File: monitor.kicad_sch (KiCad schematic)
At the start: 54 parts, among them J1 USB_C_Plug, J2 USB_C_Receptacle_USB2.0_14P, J3 Display, J4 Program, J5 Boot, U1 STM32U031K8Ux, U2 TPSM365R6V3RDNR, U3 TMP117xxDRV, U4 REF5025ADGK, U5 CC6903, Y1 32768Hz

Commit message: First cut of some code
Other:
- note added: "0x92 / 0x49 address."
- note removed: "0x90 / 0x48 address."
- moved on the sheet: C1, R1, R2
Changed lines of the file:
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@@
 	(generator_version "9.0")
 	(paper "A4")
-	(text "0x90 / 0x48 address."
+	(text "0x92 / 0x49 address."
 		(exclude_from_sim no)
 		(at 155.956 133.35 0)
@@
 	)
 	(junction
-		(at 134.62 52.07)
+		(at 135.89 53.34)
 		(diameter 0)
 		(color 0 0 0 0)
@@
 	)
 	(junction
-		(at 128.27 52.07)
+		(at 129.54 53.34)
 		(diameter 0)
 		(color 0 0 0 0)
@@
 	)
 	(junction
-		(at 128.27 60.96)
+		(at 129.54 62.23)
 		(diameter 0)
 		(color 0 0 0 0)
@@
 	(wire
 		(pts
-			(xy 128.27 60.96) (xy 134.62 60.96)
+			(xy 129.54 62.23) (xy 135.89 62.23)
 		)
 		(stroke
@@
 	(wire
 		(pts
-			(xy 134.62 52.07) (xy 134.62 53.34)
+			(xy 135.89 53.34) (xy 135.89 54.61)
 		)
 		(stroke
@@
 	(wire
 		(pts
-			(xy 128.27 52.07) (xy 134.62 52.07)
+			(xy 129.54 53.34) (xy 135.89 53.34)
 		)
 		(stroke
@@
 	(wire
 		(pts
-			(xy 128.27 52.07) (xy 128.27 53.34)
+			(xy 129.54 53.34) (xy 129.54 54.61)
 		)
 		(stroke
@@
 	(wire
 		(pts
-			(xy 134.62 52.07) (xy 137.16 52.07)
+			(xy 135.89 53.34) (xy 138.43 53.34)
 		)
 		(stroke
@@
 	(wire
 		(pts
-			(xy 114.3 52.07) (xy 120.65 52.07)
+			(xy 115.57 53.34) (xy 121.92 53.34)
 		)
 		(stroke
@@
 	)
 	(label "Vout"
-		(at 114.3 52.07 0)
+		(at 115.57 53.34 0)
 		(effects
 			(font
@@
 	)
 	(label "VSense"
-		(at 137.16 52.07 180)
+		(at 138.43 53.34 180)
 		(effects
 			(font
@@
 	(symbol
 		(lib_id "Device:R")
-		(at 128.27 57.15 0)
+		(at 129.54 58.42 0)
 		(unit 1)
 		(exclude_from_sim no)
@@
 		(dnp no)
 		(property "Reference" "R2"
-			(at 127 57.1499 90)
+			(at 128.27 58.4199 90)
 			(do_not_autoplace yes)
 			(effects
@@
 		)
 		(property "Value" "18k"
-			(at 128.27 57.1499 90)
+			(at 129.54 58.4199 90)
 			(effects
 				(font
@@
 		)
 		(property "Footprint" "Resistor_SMD:R_0402_1005Metric"
-			(at 126.492 57.15 90)
+			(at 127.762 58.42 90)
 			(effects
 				(font
@@
 		)
 		(property "Datasheet" "~"
-			(at 128.27 57.15 0)
+			(at 129.54 58.42 0)
 			(effects
 				(font
@@
 		)
 		(property "Description" "Resistor"
-			(at 128.27 57.15 0)
+			(at 129.54 58.42 0)
 			(effects
 				(font
@@
 		)
 		(property "JLCPCB" "C25762"
-			(at 128.27 57.15 0)
+			(at 129.54 58.42 0)
 			(effects
 				(font
@@
 	(symbol
 		(lib_id "power:GND")
-		(at 128.27 60.96 0)
+		(at 129.54 62.23 0)
 		(unit 1)
 		(exclude_from_sim no)
@@
 		(dnp no)
 		(property "Reference" "#PWR053"
-			(at 128.27 67.31 0)
+			(at 129.54 68.58 0)
 			(effects
 				(font
@@
 		)
 		(property "Value" "GND"
-			(at 128.27 64.516 0)
+			(at 129.54 65.786 0)
 			(effects
 				(font
@@
 		)
 		(property "Footprint" ""
-			(at 128.27 60.96 0)
+			(at 129.54 62.23 0)
 			(effects
 				(font
@@
 		)
 		(property "Datasheet" ""
-			(at 128.27 60.96 0)
+			(at 129.54 62.23 0)
 			(effects
 				(font
@@
 		)
 		(property "Description" "Power symbol creates a global label with name \"GND\" , ground"
-			(at 128.27 60.96 0)
+			(at 129.54 62.23 0)
 			(effects
 				(font
@@
 	(symbol
 		(lib_id "Device:C")
-		(at 134.62 57.15 0)
+		(at 135.89 58.42 0)
 		(unit 1)
 		(exclude_from_sim no)
@@
 		(dnp no)
 		(property "Reference" "C1"
-			(at 135.128 55.1179 0)
+			(at 136.398 56.3879 0)
 			(effects
 				(font
@@
 		)
 		(property "Value" "10u"
-			(at 135.382 59.4359 0)
+			(at 136.652 60.7059 0)
 			(effects
 				(font
@@
 		)
 		(property "Footprint" "Capacitor_SMD:C_0402_1005Metric"
-			(at 135.5852 60.96 0)
+			(at 136.8552 62.23 0)
 			(effects
 				(font
@@
 		)
 		(property "Datasheet" "~"
-			(at 134.62 57.15 0)
+			(at 135.89 58.42 0)
 			(effects
 				(font
@@
 		)
 		(property "Description" "Unpolarized capacitor"
-			(at 134.62 57.15 0)
+			(at 135.89 58.42 0)
 			(effects
 				(font
@@
 		)
 		(property "JLCPCB" "C15525"
-			(at 134.62 57.15 0)
+			(at 135.89 58.42 0)
 			(effects
 				(font
@@
 	(symbol
 		(lib_id "Device:R")
-		(at 124.46 52.07 90)
+		(at 125.73 53.34 90)
 		(mirror x)
 		(unit 1)
@@
 		(dnp no)
 		(property "Reference" "R1"
-			(at 124.4599 50.8 90)
+			(at 125.7299 52.07 90)
 			(do_not_autoplace yes)
 			(effects
@@
 		)
 		(property "Value" "100k"
-			(at 124.4599 52.07 90)
+			(at 125.7299 53.34 90)
 			(effects
 				(font
@@
 		)
 		(property "Footprint" "Resistor_SMD:R_0402_1005Metric"
-			(at 124.46 50.292 90)
+			(at 125.73 51.562 90)
 			(effects
 				(font
@@
 		)
 		(property "Datasheet" "~"
-			(at 124.46 52.07 0)
+			(at 125.73 53.34 0)
 			(effects
 				(font
@@
 		)
 		(property "Description" "Resistor"
-			(at 124.46 52.07 0)
+			(at 125.73 53.34 0)
 			(effects
 				(font
@@
 		)
 		(property "JLCPCB" "C25741"
-			(at 124.46 52.07 0)
+			(at 125.73 53.34 0)
 			(effects
 				(font

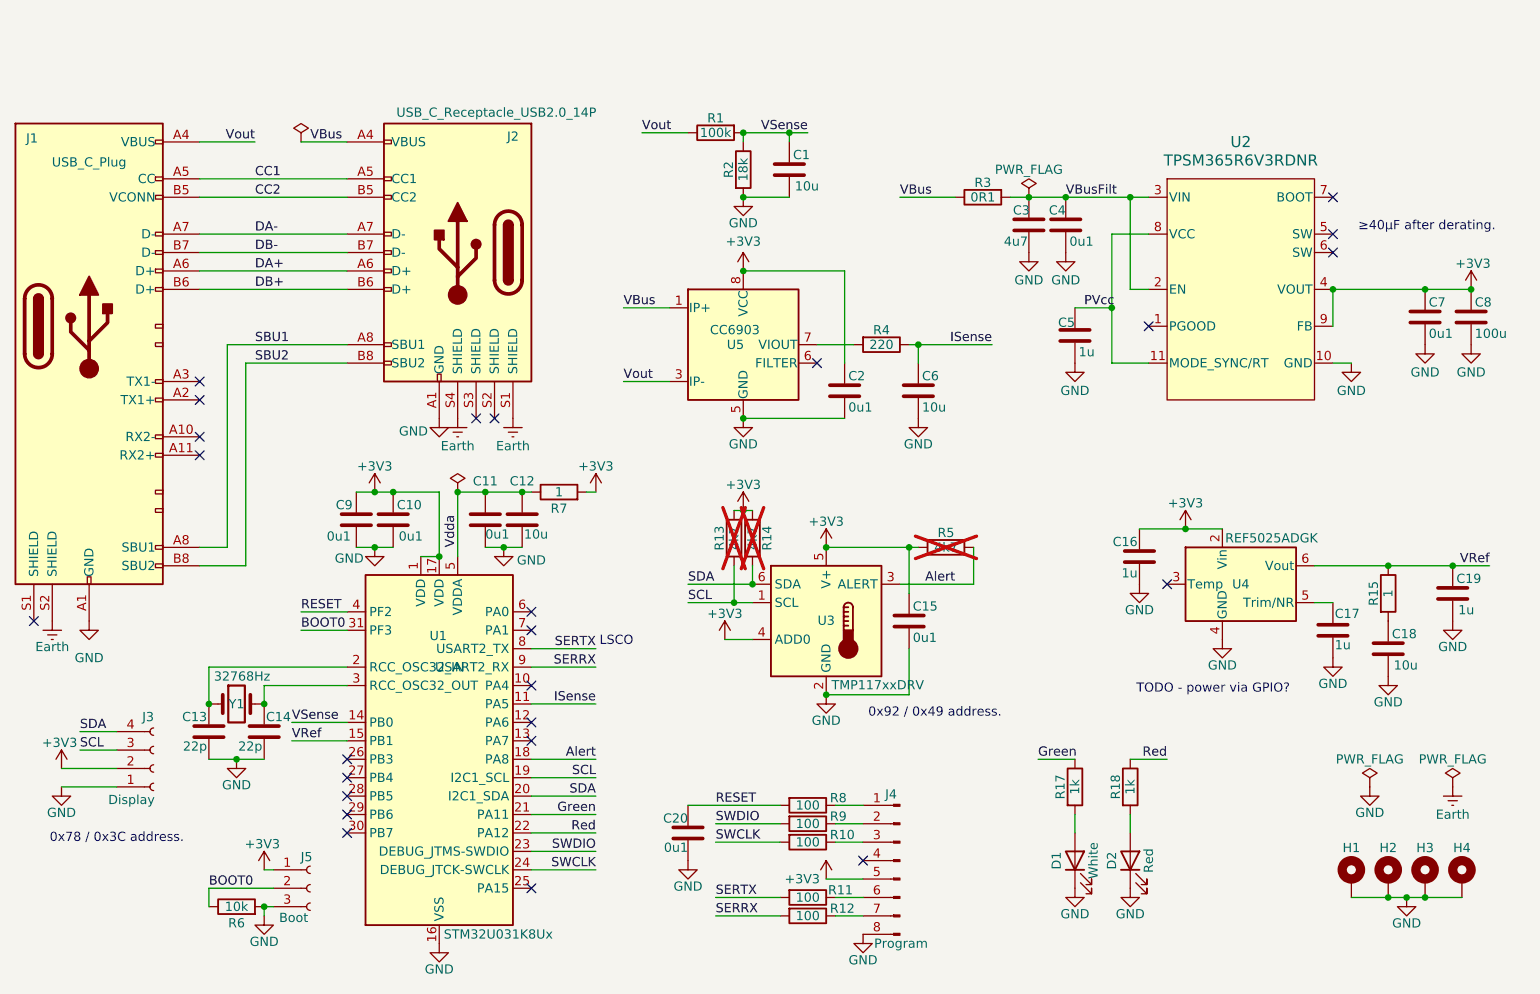
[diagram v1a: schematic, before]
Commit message: Big update to the monitor.
Accell, low side current sense.
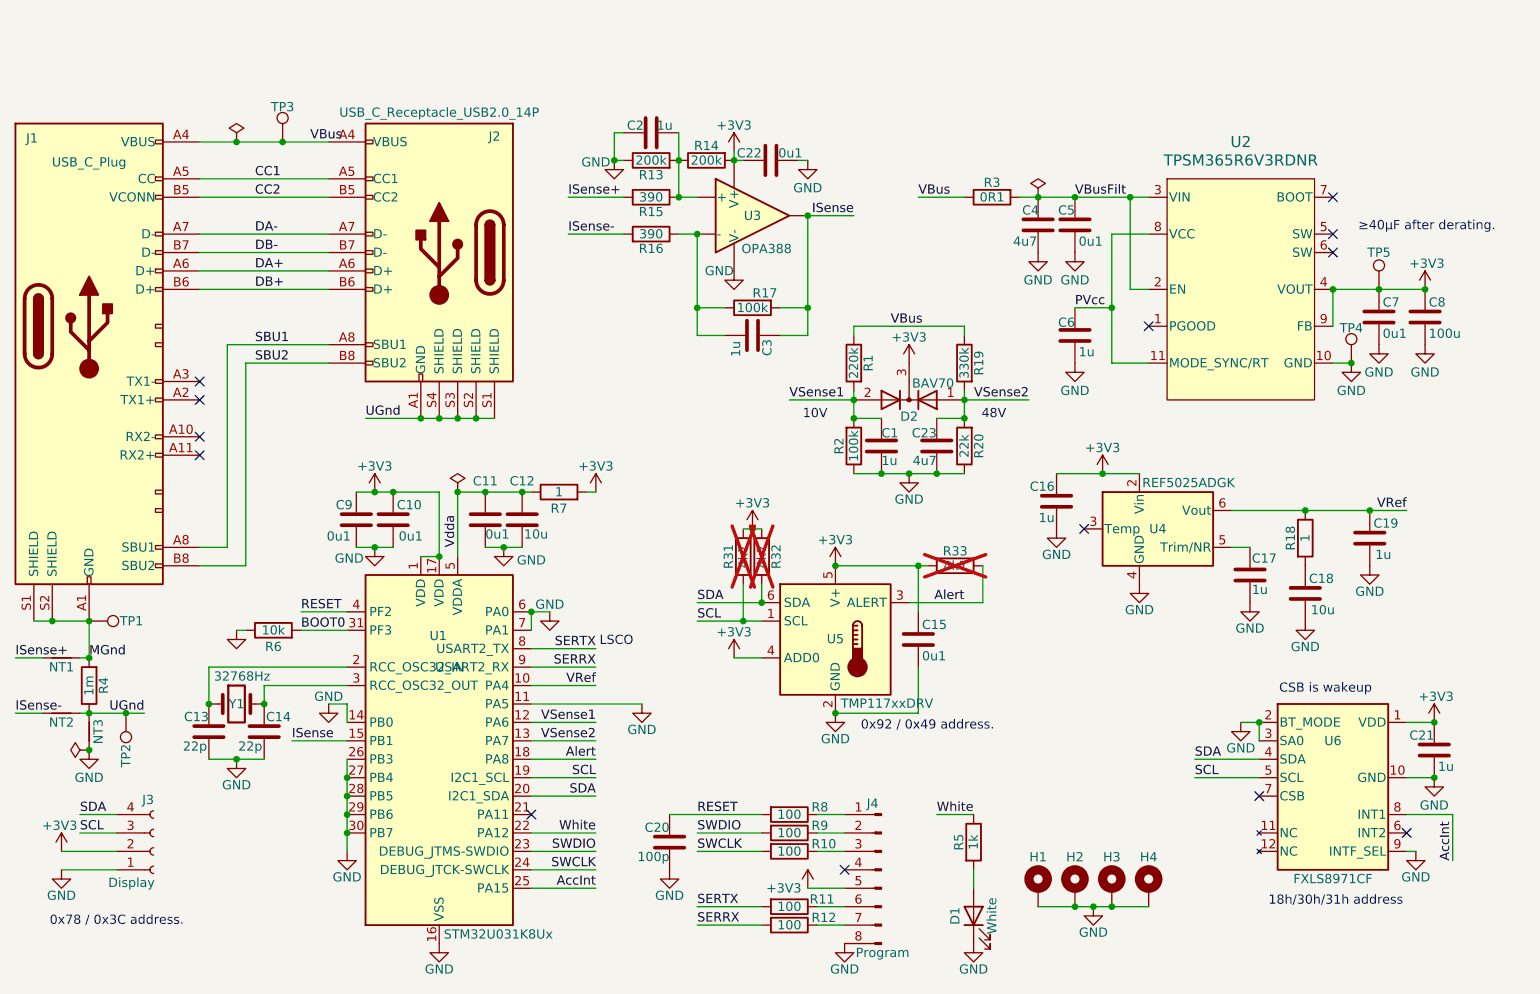
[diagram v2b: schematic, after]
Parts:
- removed C6: 10u, Capacitor_SMD:C_0402_1005Metric, symbol Device:C
- removed D2: Red, LED_SMD:LED_0603_1608Metric, symbol Device:LED
- removed J5: Boot, Parts:PinHeader_1x03_P2.54mm_Vertical, symbol Connector:Conn_01x03_Socket
- removed R18: 1k, Resistor_SMD:R_0402_1005Metric, symbol Device:R
- removed U5: CC6903, Package_SO:SOIC-8_3.9x4.9mm_P1.27mm, symbol Parts:CC6903
- added C21, C3: 1u, Capacitor_SMD:C_0402_1005Metric, symbol Device:C
- added C22: 0u1, Capacitor_SMD:C_0402_1005Metric, symbol Device:C
- added C23: 4u7, Capacitor_SMD:C_0402_1005Metric, symbol Device:C
- added D2: BAV70, Package_TO_SOT_SMD:SOT-23, symbol Diode:BAV70
- added NT1, NT2: NetTie_2, Parts:NetTie-2_0.2mm, symbol Parts:NetTie_2
- added NT3: NetTie_2, NetTie:NetTie-2_SMD_Pad0.5mm, symbol Parts:NetTie_2
- added R13, R14: 200k, Resistor_SMD:R_0603_1608Metric, symbol Device:R
- added R15, R16: 390, Resistor_SMD:R_0603_1608Metric, symbol Device:R
- added R17: 100k, Resistor_SMD:R_0603_1608Metric, symbol Device:R
- added R19: 330k, Resistor_SMD:R_0603_1608Metric, symbol Device:R
- added R20: 22k, Resistor_SMD:R_0603_1608Metric, symbol Device:R
- added TP1, TP2, TP3, TP4, TP5: TestPoint, Parts:TestPoint, symbol Connector:TestPoint
- added U3: OPA388, Package_TO_SOT_SMD:SOT-23-5, symbol Parts:OPA388
- added U6: FXLS8971CF, Parts:FXLS8971CF, symbol Parts:FXLS8971CF
- C1: value 10u -> 1u; JLCPCB C15525 -> (none)
- C2: value 0u1 -> 1u; JLCPCB C307331 -> (none)
- C20: value 0u1 -> 100p; JLCPCB C307331 -> C1546
- J3: footprint Parts:PinHeader_1x04_P2.54mm_Vertical -> Parts:JST_XH_B4B-XH-A_1x04_P2.50mm_Vertical
- R1: value 100k -> 220k; footprint Resistor_SMD:R_0402_1005Metric -> Resistor_SMD:R_0603_1608Metric; JLCPCB C25741 -> (none)
- R18: renamed from R15; footprint Resistor_SMD:R_0603_1608Metric -> Resistor_SMD:R_0402_1005Metric; JLCPCB C22936 -> C25086
- R2: value 18k -> 100k; footprint Resistor_SMD:R_0402_1005Metric -> Resistor_SMD:R_0603_1608Metric; JLCPCB C25762 -> (none)
- R4: value 220 -> 1m; footprint Resistor_SMD:R_0402_1005Metric -> Resistor_SMD:R_1206_3216Metric; JLCPCB C25091 -> (none)
- U1: now in the parts list
- renumbered C3 to C4, C4 to C5, C5 to C6, R13 to R31, R14 to R32, R5 to R33, R17 to R5, U3 to U5
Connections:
- net Vout is gone; now on net VBus: J1.A4 (VBUS), J1.A9 (VBUS), J1.B4 (VBUS), J1.B9 (VBUS), R1.1
- net +3V3: now also C21.1, C22.2, D2.3 (K), R14.2, TP5.1, U3.5 (V+), U6.1 (VDD); no longer C2.1
- net BOOT0: now also R6.2; no longer R6.1
- net GND: now also C2.1, R2.1, R6.1, U1.11 (PA5), U1.14 (PB0), U1.26 (PB3), U1.27 (PB4), U1.28 (PB5), U1.29 (PB6), U1.30 (PB7), U1.6 (PA0), U1.7 (PA1), C21.2, C22.1, C23.2, NT3.1, R13.1, R20.1, TP4.1, U3.2 (V-), U6.10 (GND), U6.2 (BT_MODE), U6.3 (SA0), U6.9 (INTF_SEL); no longer C2.2, J1.A1 (GND), J1.A12 (GND), J1.B1 (GND), J1.B12 (GND), J2.A1 (GND), J2.A12 (GND), J2.B1 (GND), J2.B12 (GND), R2.2, R6.2
- net ISense: now also U1.15 (PB1), C3.1, R17.2, U3.1; no longer R4.1, U1.11 (PA5)
- net SCL: now also U6.5 (SCL)
- net SDA: now also U6.4 (SDA)
- net VBus: now also R19.1, TP3.1
- net VRef: now also U1.10 (PA4); no longer U1.15 (PB1)
- net UGnd: now reaches J2.S2 (SHIELD)
- net UGnd: now also J2.A1 (GND), J2.A12 (GND), J2.B1 (GND), J2.B12 (GND), J2.S1 (SHIELD), J2.S3 (SHIELD), J2.S4 (SHIELD), R4.1, NT2.1, NT3.2, TP2.1
- net VSense1: now reaches U1.12 (PA6)
- net VSense1: now also C1.1, R1.2, R2.2, D2.2 (A)
- net VSense2: now reaches U1.13 (PA7)
- net VSense2: now also C23.1, D2.1 (A), R19.2, R20.2
- net AccInt: now reaches U1.25 (PA15)
- net AccInt: now also U6.8 (INT1)
- net MGnd: now reaches R4.2
- net MGnd: now also J1.A1 (GND), J1.A12 (GND), J1.B1 (GND), J1.B12 (GND), J1.S1 (SHIELD), J1.S2 (SHIELD), NT1.1, TP1.1
- removed net Earth: J1.S2 (SHIELD), J2.S1 (SHIELD), J2.S4 (SHIELD)
- net Green: no longer names the net of U1.21 (PA11)
- net Green: no longer R5.1
- net Red renamed White
- net White: now also R5.1
- removed net VSense: C1.1, R1.2, R2.1, U1.14 (PB0)
- new net: C2.2, R13.2, R14.1, R15.1, U3.3 (+)
- new net: C3.2, R16.1, R17.1, U3.4 (-)
- new net ISense+: NT1.2, R15.2
- new net ISense-: NT2.2, R16.2
- no-connect marks 25 -> 13
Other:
- note added: "10V"
- note added: "18h/30h/31h address"
- note added: "48V"
- note added: "CSB is wakeup"
- note removed: "TODO - power via GPIO?"
- moved on the sheet: C1, C15, C16, C17, C18, C19, C20, C4, C5, C7, C8, D1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

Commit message: Switch to the 2-stage sense amp.
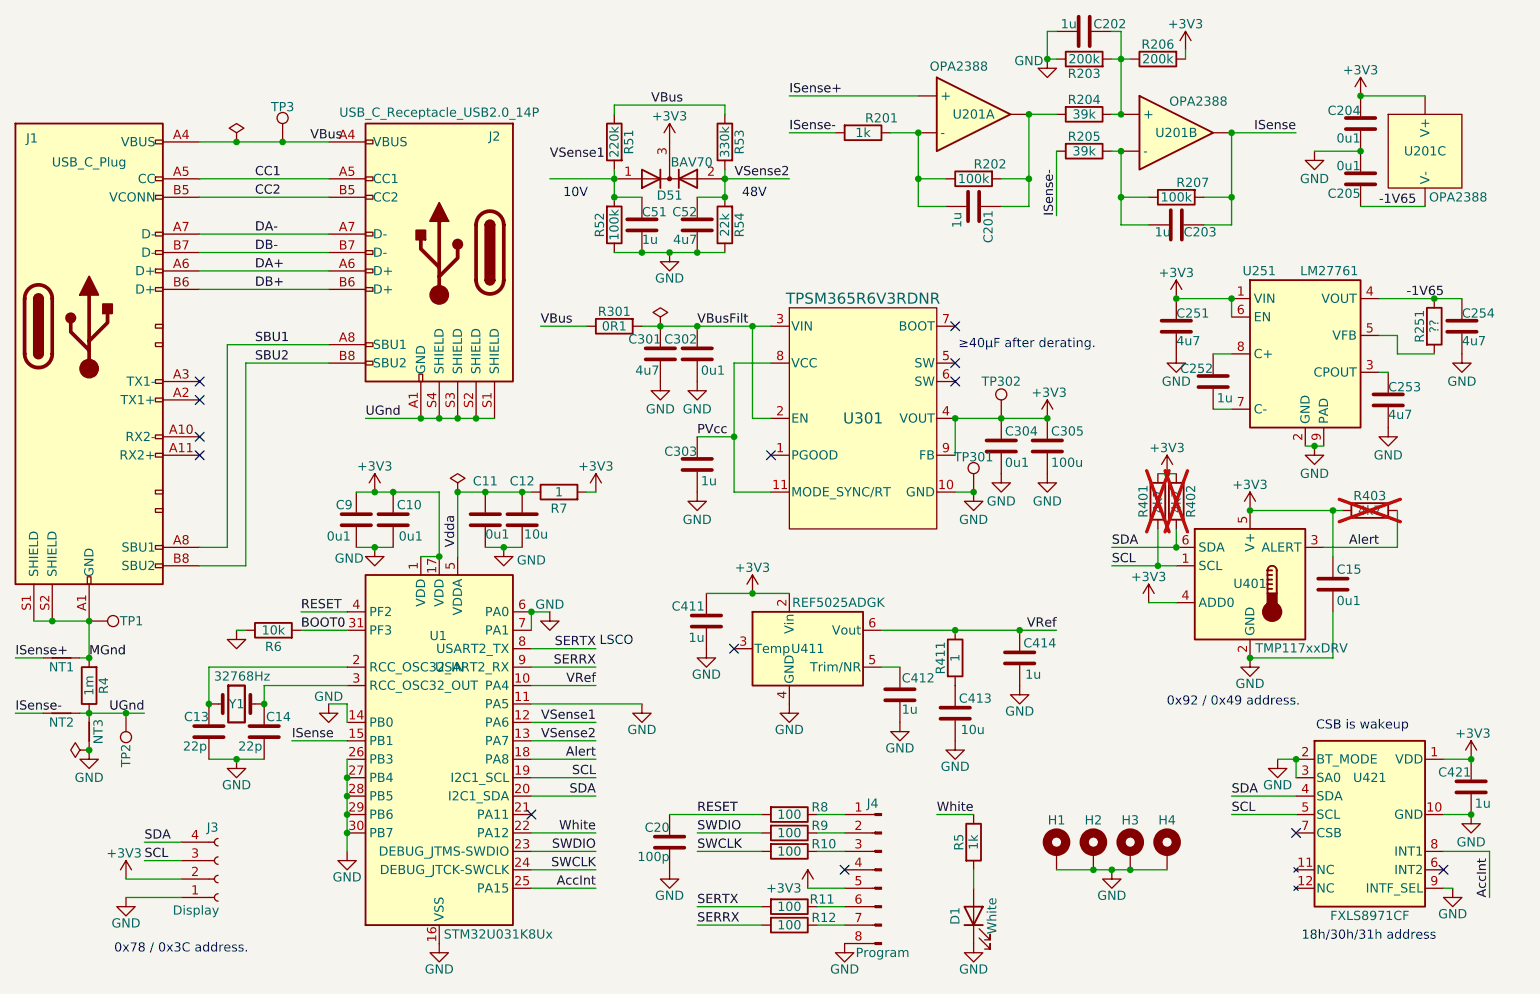
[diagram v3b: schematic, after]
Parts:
- removed C22: 0u1, Capacitor_SMD:C_0402_1005Metric, symbol Device:C
- removed R15, R16: 390, Resistor_SMD:R_0603_1608Metric, symbol Device:R
- removed U3: OPA388, Package_TO_SOT_SMD:SOT-23-5, symbol Parts:OPA388
- added C202, C252: 1u, Capacitor_SMD:C_0402_1005Metric, symbol Device:C
- added C204, C205: 0u1, Capacitor_SMD:C_0402_1005Metric, symbol Device:C
- added C251, C253, C254: 4u7, Capacitor_SMD:C_0402_1005Metric, symbol Device:C
- added R201: 1k, Resistor_SMD:R_0603_1608Metric, symbol Device:R
- added R204, R205: 39k, Resistor_SMD:R_0603_1608Metric, symbol Device:R
- added R207: 100k, Resistor_SMD:R_0603_1608Metric, symbol Device:R
- added R251: ??, Resistor_SMD:R_0603_1608Metric, symbol Device:R
- added U201: OPA2388, Package_SO:MSOP-8_3x3mm_P0.65mm, symbol Parts:OPA2388
- added U251: LM27761, Package_SON:WSON-8-1EP_2x2mm_P0.5mm_EP0.9x1.6mm, symbol Regulator_SwitchedCapacitor:LM27761
- renumbered C3 to C201, C2 to C203, C4 to C301, C5 to C302, C6 to C303, C7 to C304, C8 to C305, C16 to C411, C17 to C412, C18 to C413, C19 to C414, C21 to C421, C1 to C51, C23 to C52, D2 to D51, R17 to R202, R13 to R203, R14 to R206, R3 to R301, R31 to R401, R32 to R402, R33 to R403, R18 to R411, R1 to R51, R2 to R52, R19 to R53, R20 to R54, TP4 to TP301, TP5 to TP302, U2 to U301, U5 to U401, U4 to U411, U6 to U421
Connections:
- net +3V3: now also C204.1, C251.1, U201.8 (V+), U251.1 (VIN), U251.6 (EN)
- net GND: now also C202.2, C204.2, C205.1, C251.2, C253.2, C254.2, U251.2 (GND), U251.9 (PAD); no longer C203.1
- net ISense: now also C203.1, R207.2, U201.7; no longer C201.1, R202.2
- net ISense+: now also U201.3 (+)
- net ISense-: now also R201.2, R205.2
- net VSense1: no longer C51.1, D51.2 (A), R51.2, R52.2
- net VSense2: now also D51.2 (A); no longer D51.1 (A)
- net at R203.2, R206.1: now also C202.1, R204.1, U201.5 (+); no longer C203.2
- net at C201.2, R202.1: now also R201.1, U201.2 (-)
- new net: C252.1, U251.8 (C+)
- new net: C252.2, U251.7 (C-)
- new net: C203.2, R205.1, R207.1, U201.6 (-)
- new net: C51.1, D51.1 (A), R51.2, R52.2
- new net: C253.1, U251.3 (CPOUT)
- new net: R251.2, U251.5 (VFB)
- new net: C201.1, R202.2, R204.2, U201.1
- new net -1V65: C205.2, C254.1, R251.1, U201.4 (V-), U251.4 (VOUT)
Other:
- moved on the sheet: C15, C201, C203, C301, C302, C303, C304, C305, C411, C412, C413, C414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
